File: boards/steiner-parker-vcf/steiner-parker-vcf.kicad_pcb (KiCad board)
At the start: 2 copper layers, 44 x 86 mm, 78 parts, among them J1 Eurorack Power, J2 S1711-46R, J3 Conn_02x08_Odd_Even, J4 S1711-46R, Q1 BC547B, Q2 BC547B, U1 TL072, U2 TL072, U3 TL072

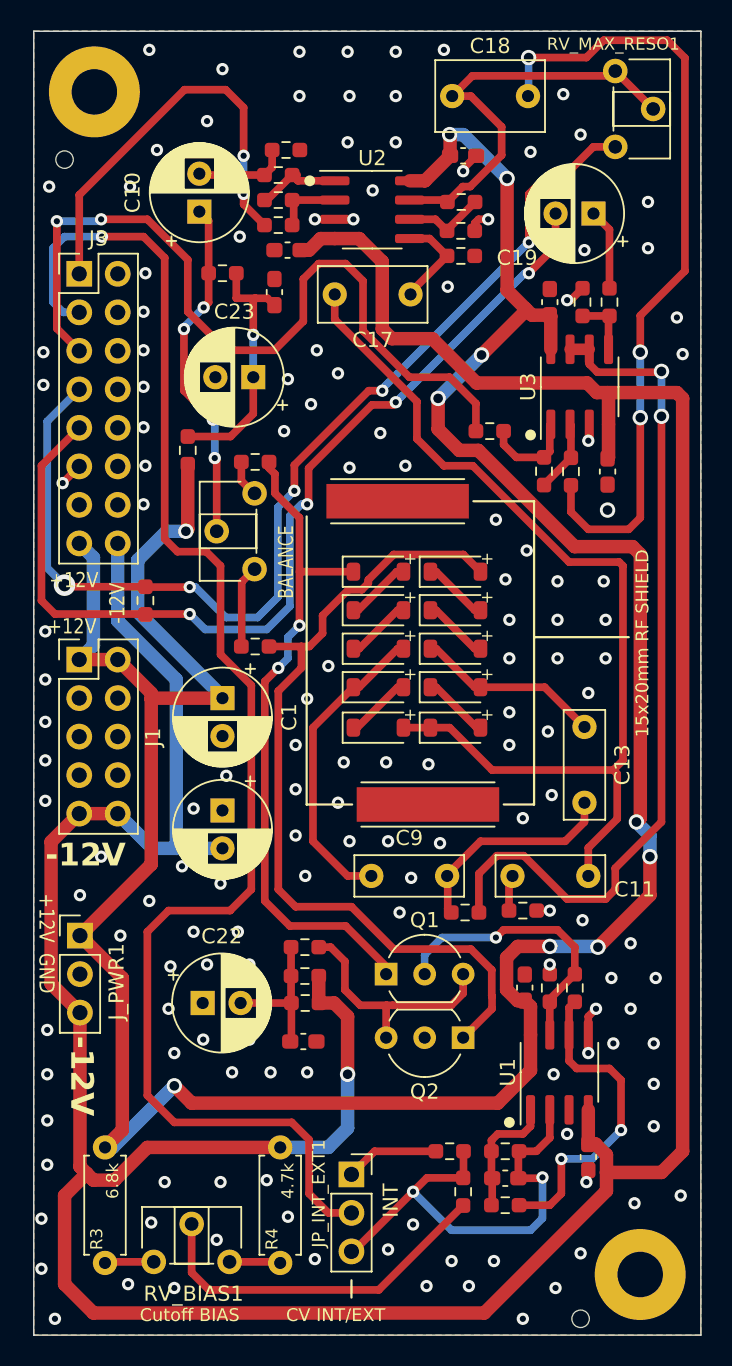
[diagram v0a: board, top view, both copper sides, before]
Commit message: Updated minimum Cutoff resistance on filter
https://github.com/shmoergh/hog/issues/24

Filter: update R4 value to 3.3kΩ. This allows better minimum cutoff value
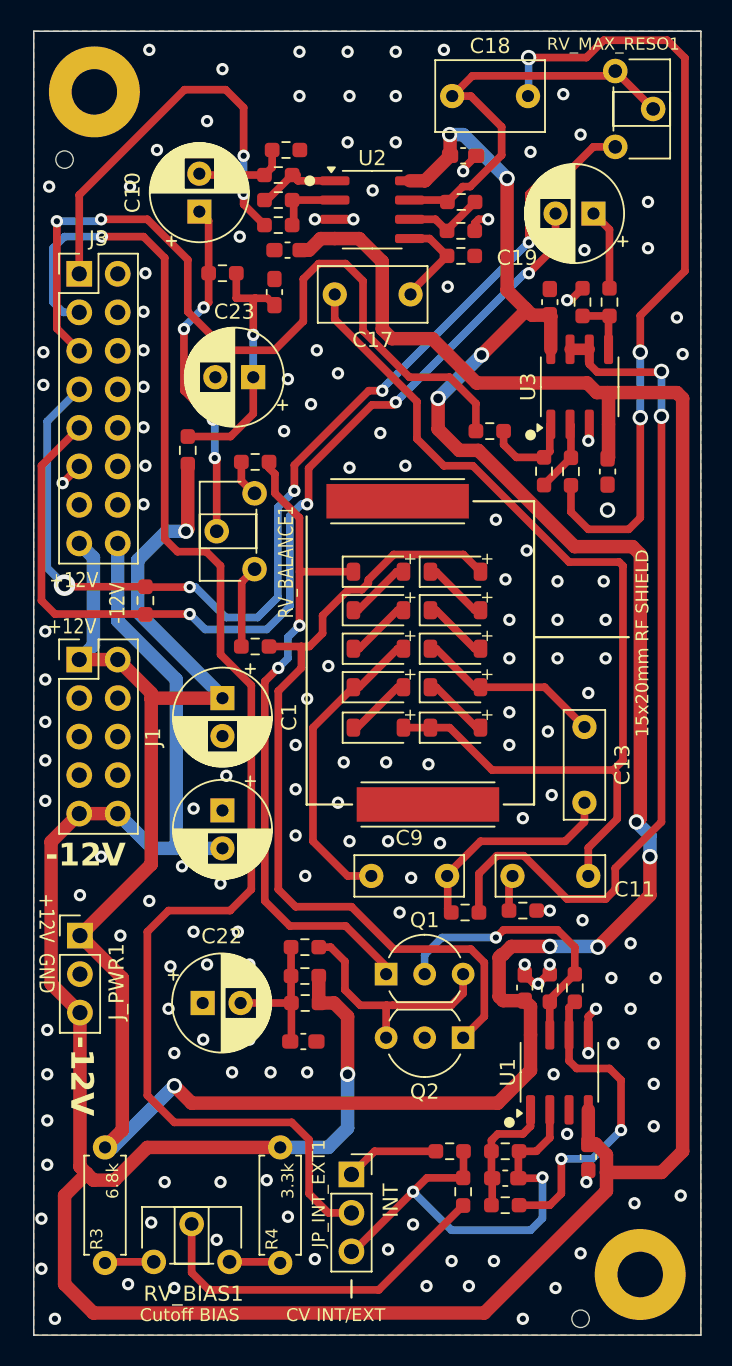
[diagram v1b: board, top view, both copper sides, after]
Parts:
- R4: value 4.7k -> 3.3k
- renumbered BALANCE to RV_BALANCE1
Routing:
- net GND: track 7.70 -> 9.87 mm, vias 152 -> 154
- net +12V: track 195.8 -> 197.1 mm

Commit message: Added production files for VCF
ref https://github.com/shmoergh/hog/issues/19
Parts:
- removed J_PWR1: Conn_01x03, Connector_PinHeader_2.54mm:PinHeader_1x03_P2.54mm_Vertical
- C1, C2, C22, C23: footprint Capacitor_THT:CP_Radial_D6.3mm_P2.50mm -> Capacitor_SMD:CP_Elec_6.3x7.7
- C10, C19: footprint Capacitor_THT:CP_Radial_D6.3mm_P2.50mm -> Capacitor_SMD:CP_Elec_4x5.4
- moved C2 14.1 mm to (130.8, 115.6)
- moved C1 5.31 mm to (138.0, 102.1)
- moved C23 1.45 mm to (142.9, 76.1), turned to 0 degrees
- moved C22 1.05 mm to (139.2, 117.1), turned to 90 degrees
- moved C10 1.05 mm to (137.7, 63.9)
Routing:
- net -12V: track 233.8 -> 226.4 mm
- net Net-(C14-Pad1): track 9.62 -> 11.7 mm
- net +12V: track 197.1 -> 195.2 mm, vias 10 -> 11
- net Net-(C10-Pad1): track 22.9 -> 22.3 mm
- net Net-(C16-Pad1): track 17.0 -> 17.4 mm, vias 1 -> 2
- net GND: vias 154 -> 159
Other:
- board text removed: "GND"
